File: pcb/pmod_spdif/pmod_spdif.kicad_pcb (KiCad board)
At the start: 2 copper layers, 36.8 x 17 mm, 17 parts, among them J1 PMOD, J2 Conn_01x06_Male, U1 74HC04, U2 CAT3200-5, U3 TOTX1350(F), U4 SN74LVC1T45DBV

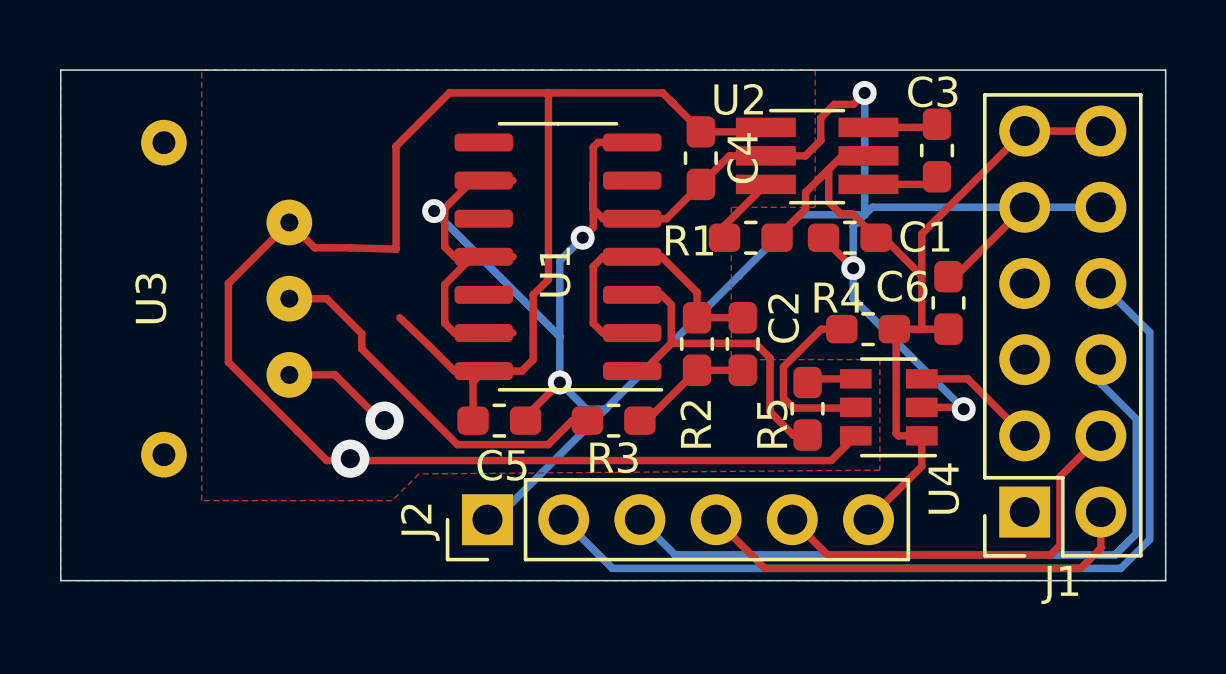
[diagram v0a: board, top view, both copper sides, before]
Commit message: pmod_spdif v2. Only cosmetic changes.
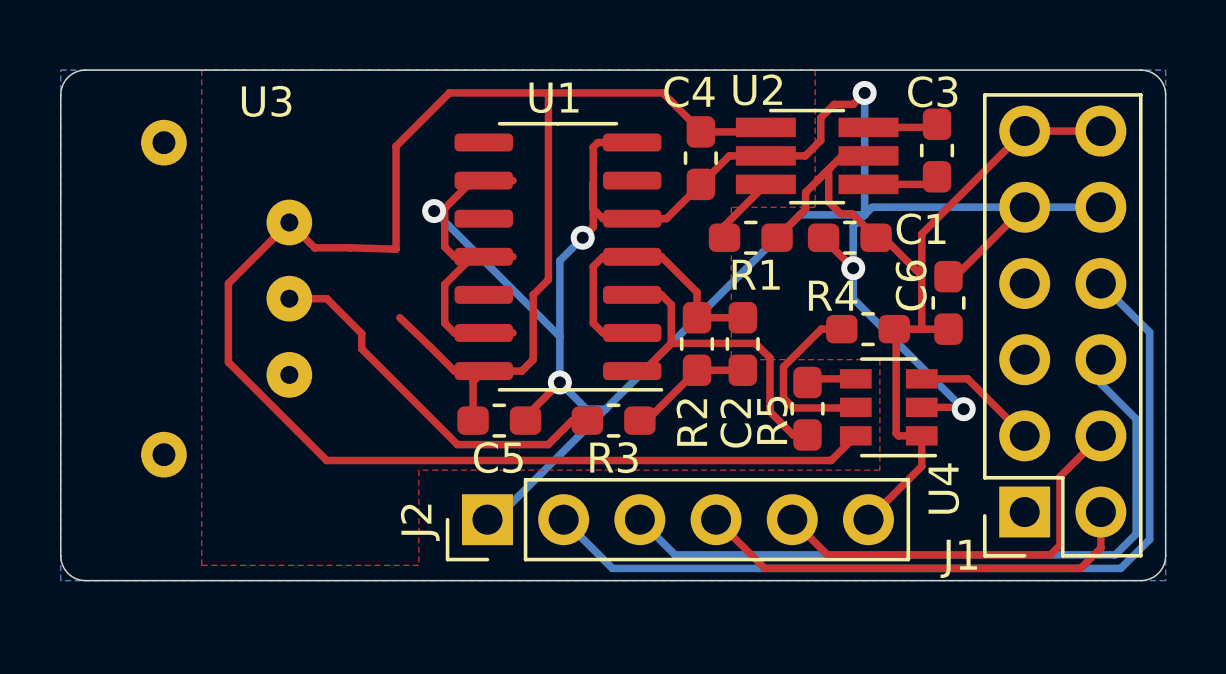
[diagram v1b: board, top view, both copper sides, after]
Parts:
- R4: value R -> 1K
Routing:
- net (no net): track 3.81 -> 0.00 mm, vias 1 -> 0
- net +5V: vias 1 -> 0
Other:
- outline, holes or cut-outs redrawn
- board text added: "3V3"
- board text added: "GND"
- board text added: "I2S_BCLK"
- board text added: "I2S_MCLK"
- board text added: "I2S_SDO"
- board text added: "I2S_WS"
- board text added: "PMOD to S/PDIF TOSLINK v2 https://github.com/tomverbeure/spdif_pmod"
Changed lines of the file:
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@@
   (general
     (thickness 1.6)
-    (drawings 4)
-    (tracks 194)
+    (drawings 15)
+    (tracks 189)
     (zones 0)
     (modules 17)
@@
     (38 B.Mask user)
     (39 F.Mask user)
-    (40 Dwgs.User user hide)
+    (40 Dwgs.User user)
     (41 Cmts.User user)
     (42 Eco1.User user)
@@
     (tags "capacitor handsolder")
     (attr smd)
-    (fp_text reference C6 (at -0.522 1.524 180) (layer F.SilkS)
+    (fp_text reference C6 (at -0.5855 1.2065 270) (layer F.SilkS)
       (effects (font (size 1 1) (thickness 0.15)))
     )
@@
   (module "custom_parts:TOTXA1350(F)" (layer F.Cu)
     (at 132.08 60.452 90)
-    (fp_text reference U3 (at 0 0.5 90) (layer F.SilkS)
+    (fp_text reference U3 (at 6.5405 4.318 180) (layer F.SilkS)
       (effects (font (size 1 1) (thickness 0.15)))
     )
@@
     (tags "TSOT-23-6 MK06A TSOT-6 Hand-soldering")
     (attr smd)
-    (fp_text reference U2 (at -2.608 -1.844 180) (layer F.SilkS)
+    (fp_text reference U2 (at -1.973 -2.1615 180) (layer F.SilkS)
       (effects (font (size 1 1) (thickness 0.15)))
     )
@@
     (tags "resistor handsolder")
     (attr smd)
-    (fp_text reference R5 (at -0.522 -1.143 90) (layer F.SilkS)
+    (fp_text reference R5 (at -0.395 -1.143 90) (layer F.SilkS)
       (effects (font (size 1 1) (thickness 0.15)))
     )
@@
     (tags "resistor handsolder")
     (attr smd)
-    (fp_text reference R4 (at -1.002 -1.016 180) (layer F.SilkS)
-      (effects (font (size 1 1) (thickness 0.15)))
-    )
-    (fp_text value R (at 0 1.43) (layer F.Fab)
+    (fp_text reference R4 (at -1.1925 -1.0795 180) (layer F.SilkS)
+      (effects (font (size 1 1) (thickness 0.15)))
+    )
+    (fp_text value 1K (at 0 1.43) (layer F.Fab)
       (effects (font (size 1 1) (thickness 0.15)))
     )
@@
     (descr "Through hole straight pin header, 2x06, 2.54mm pitch, double rows")
     (tags "Through hole pin header THT 2x06 2.54mm double row")
-    (fp_text reference J1 (at -1.27 -2.33) (layer F.SilkS)
+    (fp_text reference J1 (at 2.0955 -1.4605) (layer F.SilkS)
       (effects (font (size 1 1) (thickness 0.15)))
     )
@@
     (tags "capacitor handsolder")
     (attr smd)
-    (fp_text reference C5 (at 0.113 1.524) (layer F.SilkS)
+    (fp_text reference C5 (at -0.014 1.27) (layer F.SilkS)
       (effects (font (size 1 1) (thickness 0.15)))
     )
@@
     (tags "SOIC SO")
     (attr smd)
-    (fp_text reference U1 (at 0.065 -0.508 270) (layer F.SilkS)
+    (fp_text reference U1 (at 0.1285 5.2705) (layer F.SilkS)
       (effects (font (size 1 1) (thickness 0.15)))
     )
@@
     (tags "resistor handsolder")
     (attr smd)
-    (fp_text reference R2 (at -2.681 0 90) (layer F.SilkS)
+    (fp_text reference R2 (at -2.6175 -0.127 90) (layer F.SilkS)
       (effects (font (size 1 1) (thickness 0.15)))
     )
@@
     (tags "resistor handsolder")
     (attr smd)
-    (fp_text reference R1 (at 2.046 -0.127) (layer F.SilkS)
+    (fp_text reference R1 (at -0.1765 -1.27) (layer F.SilkS)
       (effects (font (size 1 1) (thickness 0.15)))
     )
@@
     (tags "capacitor handsolder")
     (attr smd)
-    (fp_text reference C4 (at 0 -1.43 90) (layer F.SilkS)
+    (fp_text reference C4 (at -2.173 0.381 180) (layer F.SilkS)
       (effects (font (size 1 1) (thickness 0.15)))
     )
@@
     (tags "capacitor handsolder")
     (attr smd)
-    (fp_text reference C2 (at -0.875 -1.397 90) (layer F.SilkS)
+    (fp_text reference C2 (at 2.6175 0.1905 90) (layer F.SilkS)
       (effects (font (size 1 1) (thickness 0.15)))
     )
@@
     (tags "capacitor handsolder")
     (attr smd)
-    (fp_text reference C1 (at -2.526 0) (layer F.SilkS)
+    (fp_text reference C1 (at -2.399 0.254) (layer F.SilkS)
       (effects (font (size 1 1) (thickness 0.15)))
     )
@@
     )
   )
-  (gr_line (start 166.37 69.85) (end 166.37 52.832) (layer Edge.Cuts) (width 0.05))
-  (gr_line (start 129.54 69.85) (end 166.37 69.85) (layer Edge.Cuts) (width 0.05))
-  (gr_line (start 129.54 52.832) (end 129.54 69.85) (layer Edge.Cuts) (width 0.05))
-  (gr_line (start 166.37 52.832) (end 129.54 52.832) (layer Edge.Cuts) (width 0.05))
-  (segment (start 137.16 62.992) (end 138.684 62.992) (width 0.25) (layer F.Cu) (net 0))
-  (segment (start 138.684 62.992) (end 140.208 64.516) (width 0.25) (layer F.Cu) (net 0))
-  (segment (start 140.208 64.516) (end 140.335 64.516) (width 0.25) (layer F.Cu) (net 0))
-  (via (at 140.335 64.516) (size 1.27) (drill 0.635) (layers F.Cu B.Cu) (net 0))
+  (gr_arc (start 165.5445 69.0245) (end 165.5445 69.85) (angle -90) (layer Edge.Cuts) (width 0.05))
+  (gr_arc (start 130.3655 69.0245) (end 129.54 69.0245) (angle -90) (layer Edge.Cuts) (width 0.05))
+  (gr_arc (start 130.3655 53.6575) (end 130.3655 52.832) (angle -90) (layer Edge.Cuts) (width 0.05))
+  (gr_arc (start 165.5445 53.6575) (end 166.37 53.6575) (angle -90) (layer Edge.Cuts) (width 0.05))
+  (gr_text 3V3 (at 156.464 66.167 270) (layer B.SilkS)
+    (effects (font (size 1 1) (thickness 0.15)) (justify left mirror))
+  )
+  (gr_text I2S_BCLK (at 153.924 66.294 270) (layer B.SilkS)
+    (effects (font (size 1 1) (thickness 0.15)) (justify left mirror))
+  )
+  (gr_text I2S_MCLK (at 151.384 66.294 270) (layer B.SilkS)
+    (effects (font (size 1 1) (thickness 0.15)) (justify left mirror))
+  )
+  (gr_text I2S_WS (at 148.7805 66.294 270) (layer B.SilkS)
+    (effects (font (size 1 1) (thickness 0.15)) (justify left mirror))
+  )
+  (gr_text I2S_SDO (at 146.304 66.294 270) (layer B.SilkS)
+    (effects (font (size 1 1) (thickness 0.15)) (justify left mirror))
+  )
+  (gr_text GND (at 143.764 66.2305 270) (layer B.SilkS)
+    (effects (font (size 1 1) (thickness 0.15)) (justify left mirror))
+  )
+  (gr_text "PMOD to S/PDIF TOSLINK v2\nhttps://github.com/tomverbeure/spdif_pmod" (at 147.32 55.1815) (layer B.SilkS)
+    (effects (font (size 0.762 0.762) (thickness 0.15)) (justify mirror))
+  )
+  (gr_line (start 166.37 69.0245) (end 166.37 53.6575) (layer Edge.Cuts) (width 0.05))
+  (gr_line (start 130.3655 69.85) (end 165.5445 69.85) (layer Edge.Cuts) (width 0.05))
+  (gr_line (start 129.54 53.6575) (end 129.54 69.0245) (layer Edge.Cuts) (width 0.05))
+  (gr_line (start 165.5445 52.832) (end 130.3655 52.832) (layer Edge.Cuts) (width 0.05))
   (segment (start 151.826 55.692) (end 153.044 55.692) (width 0.25) (layer F.Cu) (net 1))
   (segment (start 150.876 56.642) (end 151.826 55.692) (width 0.25) (layer F.Cu) (net 1))
@@
   (segment (start 135.128 59.944) (end 135.128 62.568762) (width 0.25) (layer F.Cu) (net 5))
   (segment (start 137.435119 64.875881) (end 138.405248 65.84601) (width 0.25) (layer F.Cu) (net 5))
-  (via (at 139.192 65.786) (size 1.27) (drill 0.635) (layers F.Cu B.Cu) (net 5))
   (segment (start 150.876 54.864) (end 149.86 53.848) (width 0.25) (layer F.Cu) (net 5))
   (segment (start 150.876 54.892) (end 150.876 54.864) (width 0.25) (layer F.Cu) (net 5))
@@
       (pts
         (xy 154.686 57.404) (xy 151.892 57.404) (xy 151.892 62.484) (xy 156.845 62.484) (xy 156.845 66.167)
-        (xy 141.478 66.294) (xy 140.589 67.183) (xy 134.239 67.183) (xy 134.239 52.832) (xy 154.686 52.832)
+        (xy 141.478 66.167) (xy 141.478 69.342) (xy 134.239 69.342) (xy 134.239 52.832) (xy 154.686 52.832)
       )
     )
